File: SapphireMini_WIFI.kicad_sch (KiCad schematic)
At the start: 11 parts, among them M701 AdafruitWINC1500

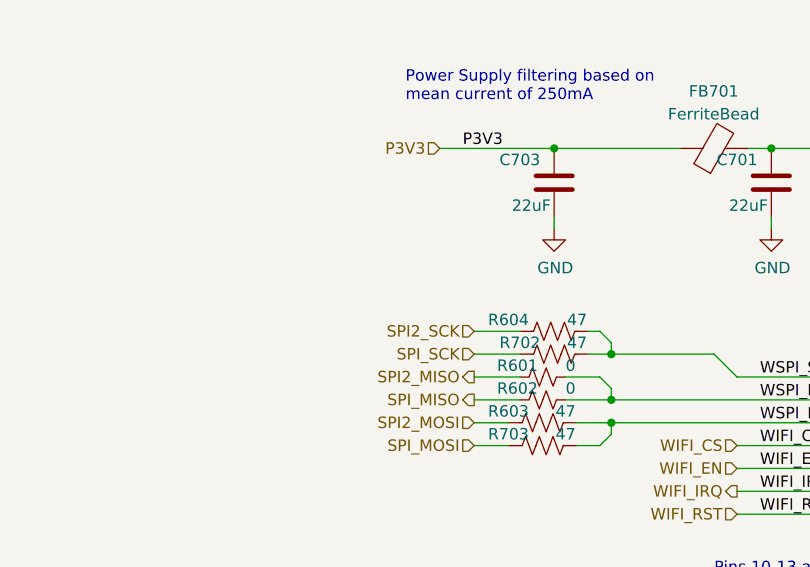
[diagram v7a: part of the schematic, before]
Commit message: Updates for Circuit Hub estimates
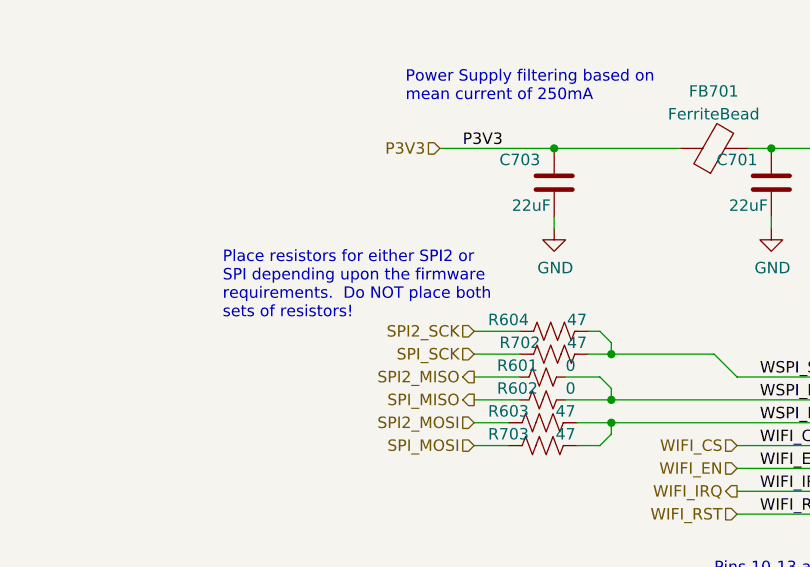
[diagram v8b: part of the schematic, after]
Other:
- note added: "Place resistors for either SPI2 or SPI depending upon the firmware requirements. Do NOT place both sets of resistors!"
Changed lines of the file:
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@@
     (stroke (width 0) (type default) (color 0 0 0 0))
+  )
+  (text "Place resistors for either SPI2 or\nSPI depending upon the firmware\nrequirements.  Do NOT place both\nsets of resistors!"
+    (at 77.47 64.77 0)
+    (effects (font (size 1.27 1.27)) (justify left bottom))
   )
   (text "Adafruit WINC1500 breakout option" (at 21.59 22.86 0)
